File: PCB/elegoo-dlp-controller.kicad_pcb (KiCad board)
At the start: 2 copper layers, 65 x 30 mm, 5 parts, among them J1 GPIO

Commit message: Add initial draft of PCB
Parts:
- added C1: 100uF, Capacitor_SMD:CP_Elec_6.3x7.7, F.Cu at (121.0, 95.0)
- added D1: D_Schottky, Diode_SMD:D_SOD-323_HandSoldering, F.Cu at (109.1, 78.4)
- added J2: Conn_01x12_Pin, Connector_Molex:Molex_Pico-Clasp_202396-1207_1x12-1MP_P1.00mm_Horizontal, F.Cu at (149.7, 94.4)
- added J3: Conn_01x08_Pin, Connector_Molex:Molex_Pico-Clasp_202396-0807_1x08-1MP_P1.00mm_Horizontal, F.Cu at (133.4, 94.3)
- added J4: Barrel_Jack, Connector_BarrelJack:BarrelJack_GCT_DCJ200-10-A_Horizontal, F.Cu at (115.0, 88.3)
- added J5: Conn_01x04_Pin, Connector_PinHeader_2.54mm:PinHeader_1x04_P2.54mm_Vertical, F.Cu at (149.0, 84.0)
- added J6: Conn_01x04_Pin, Connector_PinHeader_2.54mm:PinHeader_2x02_P2.54mm_Vertical, F.Cu at (159.8, 81.3)
- added J7: Conn_01x02_Pin, Connector_PinHeader_2.54mm:PinHeader_1x02_P2.54mm_Vertical, F.Cu at (155.8, 83.8)
- added J8: Conn_01x04_Pin, Connector_JST:JST_SH_SM04B-SRSS-TB_1x04-1MP_P1.00mm_Horizontal, F.Cu at (161.5, 88.9)
- added J9: Conn_01x01_Pin, Connector_PinHeader_2.54mm:PinHeader_1x01_P2.54mm_Vertical, F.Cu at (102.7, 78.7)
- added JP2: SolderJumper_2_Bridged, Jumper:SolderJumper-2_P1.3mm_Open_TrianglePad1.0x1.5mm, F.Cu at (115.0, 81.3)
- added TP1: TestPoint, TestPoint:TestPoint_Pad_D1.5mm, F.Cu at (125.3, 91.2)
- added U2: RECOM R-78K5.0-2.0L, Converter_DCDC:Converter_DCDC_RECOM_R-78HB-0.5L_THT, F.Cu at (119.7, 81.2)
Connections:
- J1 pad 19: /GPIO10/SPI0.MOSI -> MOSI
- J1 pad 21: /GPIO9/SPI0.MISO -> MISO
- J1 pad 22: /GPIO25 -> CSZ
- J1 pad 23: /GPIO11/SPI0.SCLK -> SCLK
- J1 pad 29: /GPIO5 -> PROJ_ON
- J1 pad 3: /GPIO2/SDA1 -> SDA
- J1 pad 31: /GPIO6 -> SYS_RDY
- J1 pad 33: /GPIO13/PWM1 -> PRINT
- J1 pad 35: /GPIO19/PCM.FS -> HOST_IRQ
- J1 pad 5: /GPIO3/SCL1 -> SCL
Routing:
- net SDA: track 0.00 -> 66.8 mm
- net +3V3: track 0.00 -> 63.5 mm
- net SCL: track 0.00 -> 61.2 mm, vias 0 -> 2
- net CSZ: track 0.00 -> 30.7 mm
- net SCLK: track 0.00 -> 30.1 mm
- net MOSI: track 0.00 -> 27.4 mm
- net MISO: track 0.00 -> 24.9 mm, vias 0 -> 1
- net PROJ_ON: track 0.00 -> 23.3 mm
- net SYS_RDY: track 0.00 -> 21.7 mm
- net PRINT: track 0.00 -> 19.8 mm
- net HOST_IRQ: track 0.00 -> 19.2 mm
- net /GPIO16: track 0.00 -> 17.8 mm
- net /GPIO20/PCM.DIN: track 0.00 -> 10.2 mm
- net /GPIO21/PCM.DOUT: track 0.00 -> 9.52 mm
- net /GPIO26: track 0.00 -> 9.01 mm
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- added copper zone on F.Cu, net +12V
- added copper zone on F.Cu, net +5V
- added copper zone on F.Cu, net /5V_raw
- added copper zone on B.Cu, net GND
- added copper zone on F.Cu, net GND
- added copper zone on F.Cu, net Net-(JP2-B)
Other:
- board text added: "12V"
- board text added: "3.3V"
- board text added: "5V"
- board text added: "Board Rev 0.1"
- board text added: "CSZ"
- board text added: "Center Positive 5.5mm OD 2.5mm ID"
- board text added: "Enable 5V"
- board text added: "GND"
- board text added: "GPIO 16"
- board text added: "GPIO 20"
- board text added: "GPIO 21"
- board text added: "GPIO 26"
- board text added: "I2C"
- board text added: "MISO"
- board text added: "MOSI"
- board text added: "Pico-Clasp 12 pin"
- board text added: "Pico-Clasp 8 pin"
- board text added: "RECOM R-78K5.0-2.0L"
- board text added: "SCLK"
- board text added: "SPI"
- board text added: "Stemma QT"
- board text added: "openMLA Project"
- board text removed: "Extend PCB edge 0.5mm if using SMT header"

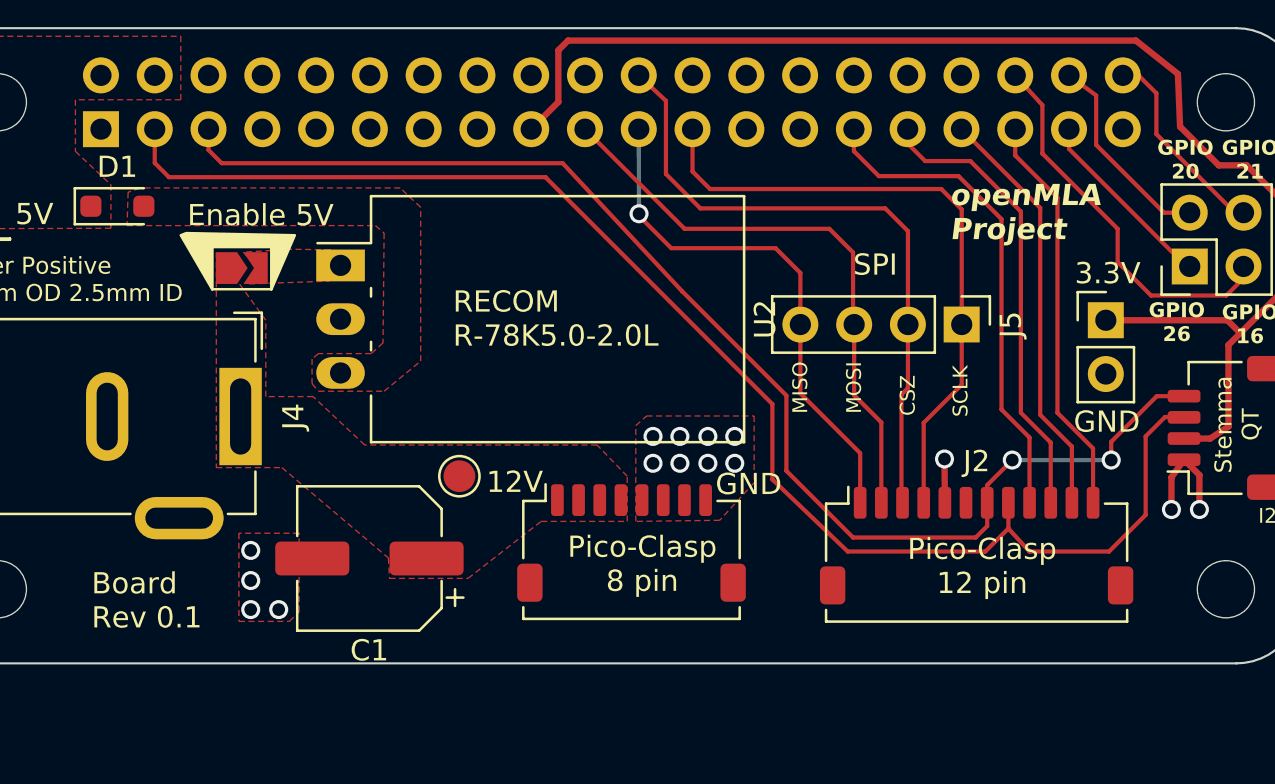
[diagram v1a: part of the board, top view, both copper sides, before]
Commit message: change dc converter and switch to vertical connectors
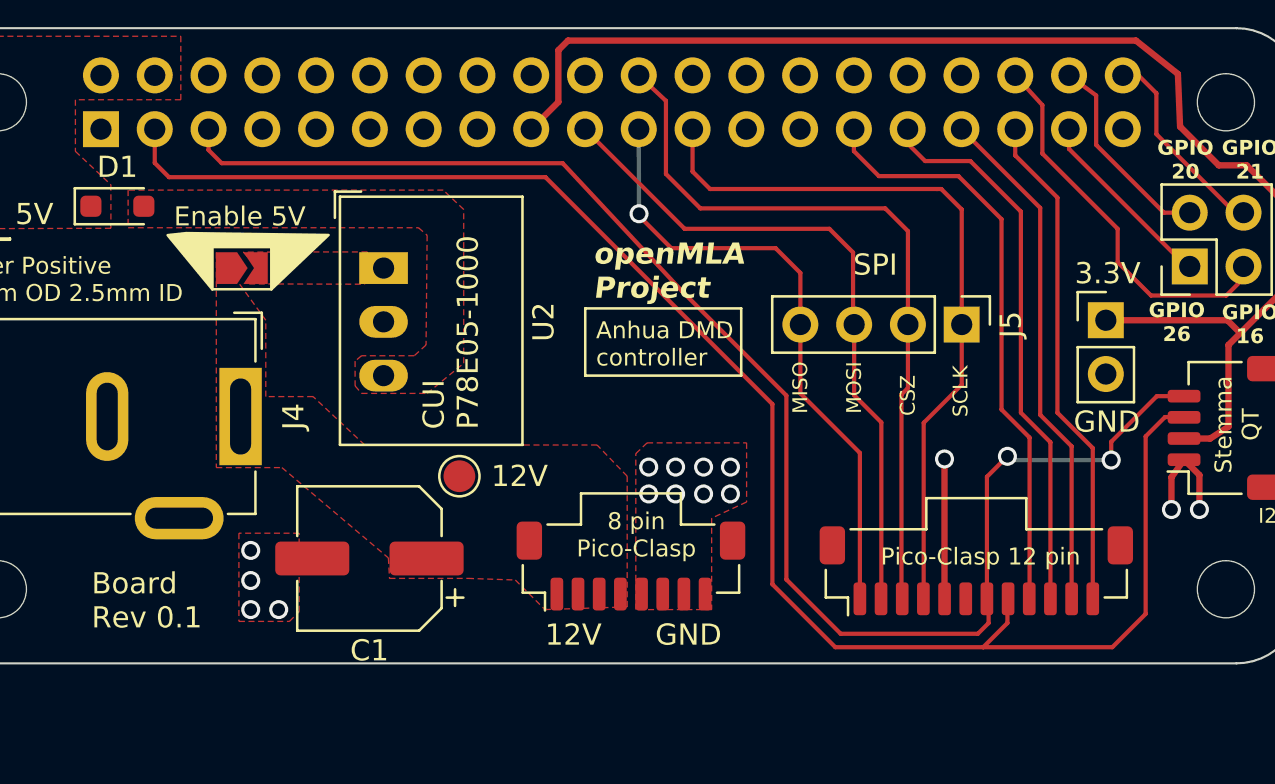
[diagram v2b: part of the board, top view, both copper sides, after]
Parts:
- added G***: LOGO, board-assets:openmla-logo, B.Cu at (134.0, 88.4)
- J2: footprint Connector_Molex:Molex_Pico-Clasp_202396-1207_1x12-1MP_P1.00mm_Horizontal -> Connector_Molex:Molex_Pico-Clasp_501331-1207_1x12-1MP_P1.00mm_Vertical
- J3: footprint Connector_Molex:Molex_Pico-Clasp_202396-0807_1x08-1MP_P1.00mm_Horizontal -> Connector_Molex:Molex_Pico-Clasp_501331-0807_1x08-1MP_P1.00mm_Vertical
- U2: value RECOM R-78K5.0-2.0L -> CUI P78E05-1000; footprint Converter_DCDC:Converter_DCDC_RECOM_R-78HB-0.5L_THT -> Converter_DCDC:Converter_DCDC_RECOM_R-78E-0.5_THT
- moved U2 2.04 mm to (121.7, 81.3)
- moved J2 1.19 mm to (149.7, 95.6)
- moved J3 1.09 mm to (133.4, 95.4)
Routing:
- net SDA: track 66.8 -> 76.9 mm
- net SCL: track 61.2 -> 71.2 mm
- net PROJ_ON: track 23.3 -> 27.8 mm
- net SCLK: track 30.1 -> 34.6 mm
- net MOSI: track 27.4 -> 32.0 mm
- net GND: track 7.27 -> 11.8 mm
- net PRINT: track 19.8 -> 24.3 mm
- net MISO: track 24.9 -> 29.4 mm
- net SYS_RDY: track 21.7 -> 26.2 mm
- net HOST_IRQ: track 19.2 -> 23.7 mm
- net CSZ: track 30.7 -> 35.3 mm
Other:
- board text added: "8 pin Pico-Clasp"
- board text added: "Anhua DMD controller"
- board text added: "CUI P78E05-1000"
- board text removed: "Pico-Clasp 8 pin"
- board text removed: "RECOM R-78K5.0-2.0L"

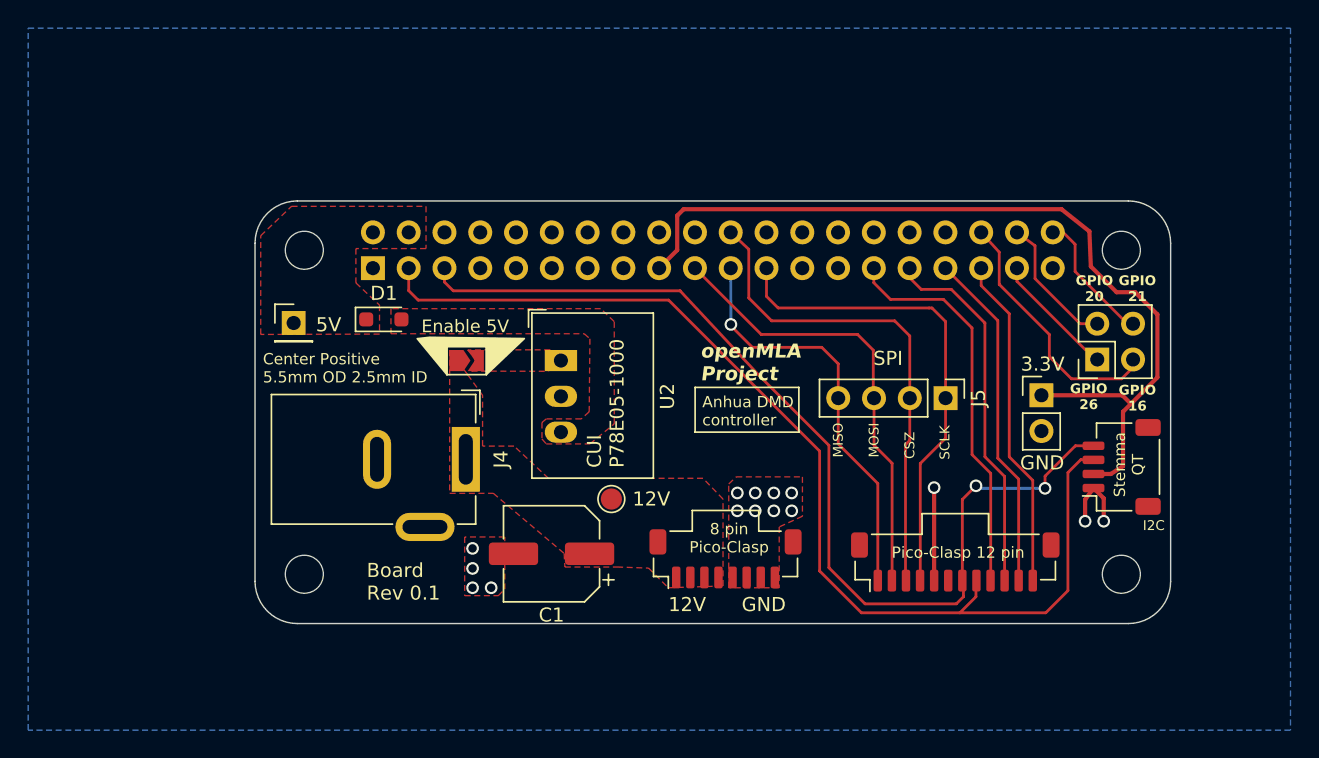
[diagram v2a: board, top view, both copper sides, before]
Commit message: Connect SPI_RDY and minor retouching
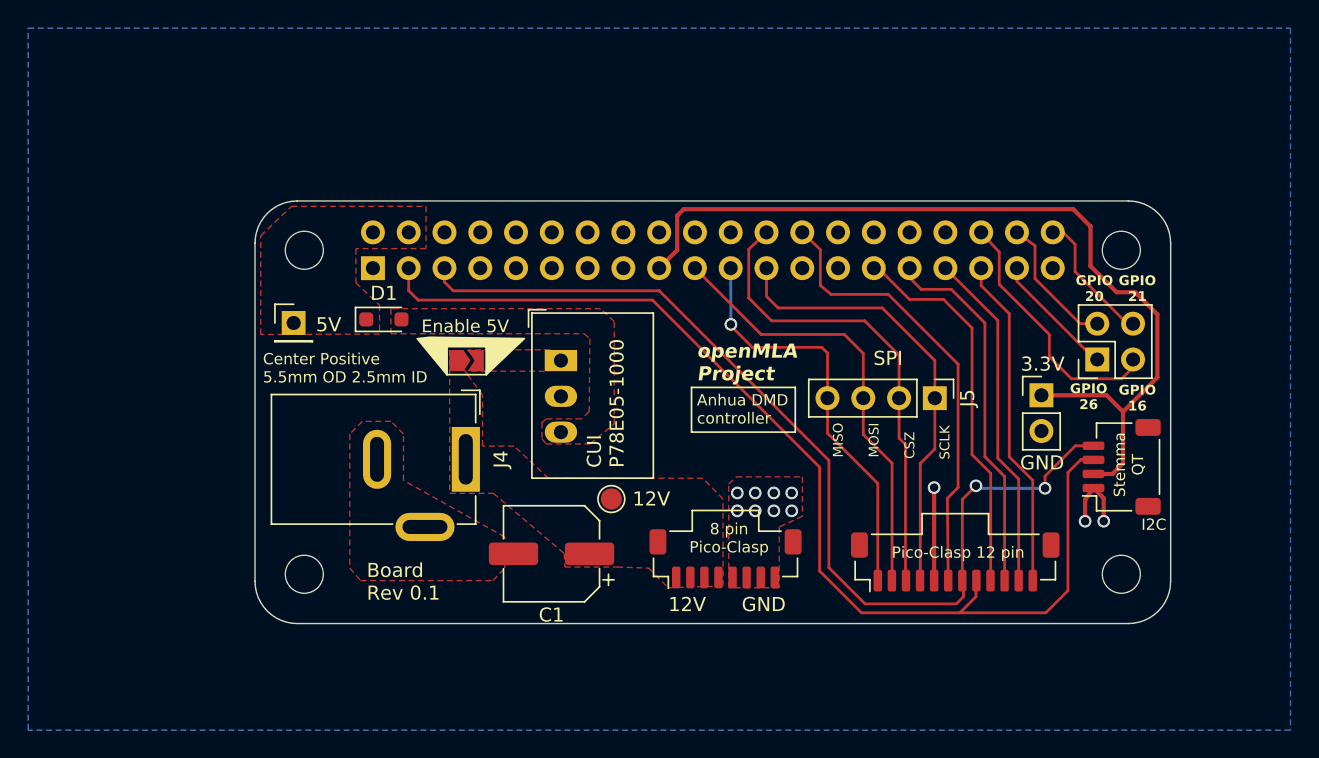
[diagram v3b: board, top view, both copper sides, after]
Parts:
- moved J5 0.76 mm to (148.3, 84.0)
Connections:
- J1 pad 22: CSZ -> /GPIO25
- J1 pad 24: /GPIO8/SPI0.CE0 -> CSZ
- J1 pad 26: /GPIO7/SPI0.CE1 -> SPI_RDY
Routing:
- net SPI_RDY: track 0.00 -> 32.1 mm
- net SCLK: track 34.6 -> 31.9 mm
- net CSZ: track 35.3 -> 33.8 mm
- net SCL: track 71.2 -> 70.4 mm
- net SDA: track 76.9 -> 76.2 mm
- net PROJ_ON: track 27.8 -> 27.2 mm
- net MOSI: track 32.0 -> 31.4 mm
- net GND: vias 15 -> 11
